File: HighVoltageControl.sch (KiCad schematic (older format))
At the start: 3 parts, among them Q1 DMG2302U, U1 NCS1S1203SC

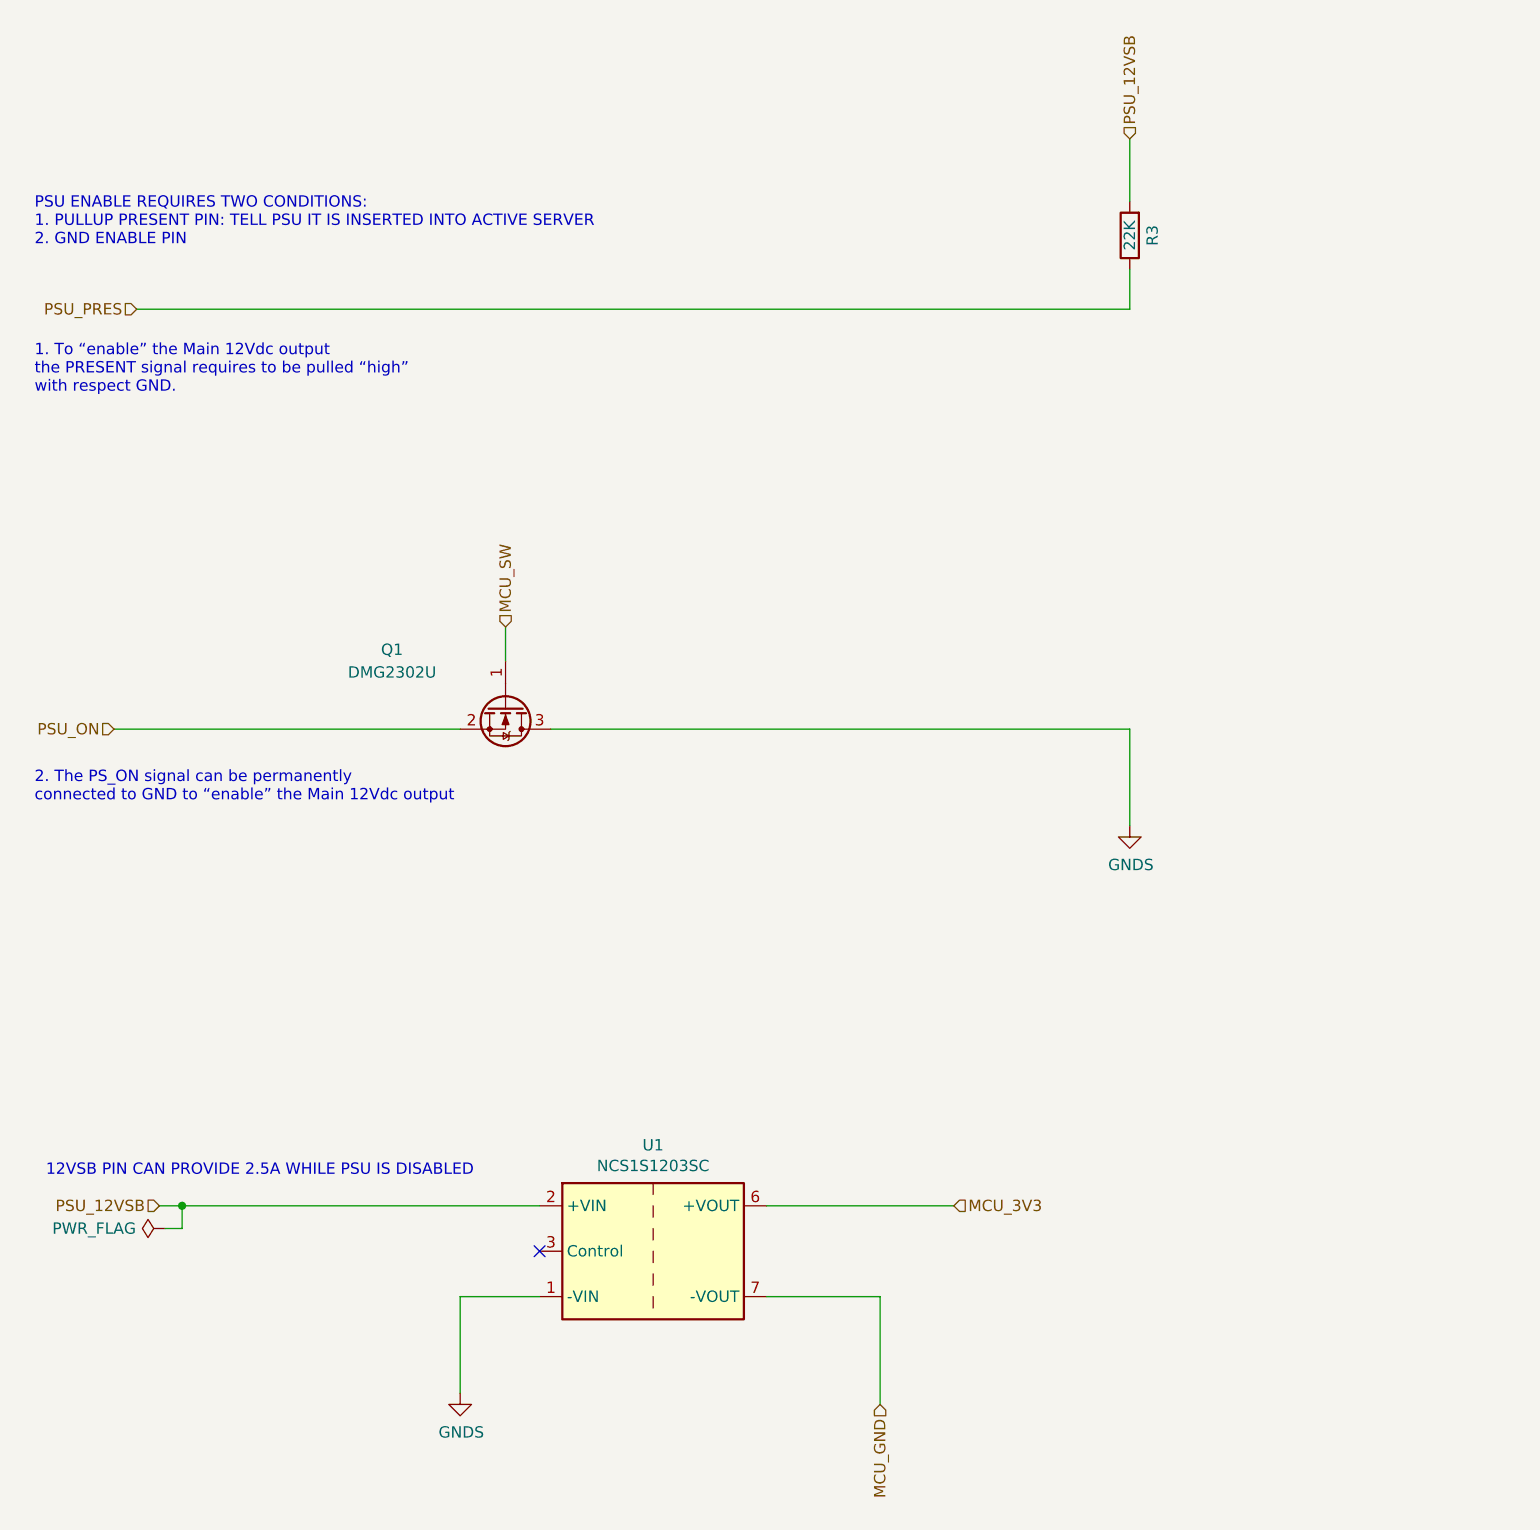
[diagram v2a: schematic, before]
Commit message: Added TFT Delayed Reset sub circuit
changed NCS1S1203SC to NCS1S1205SC
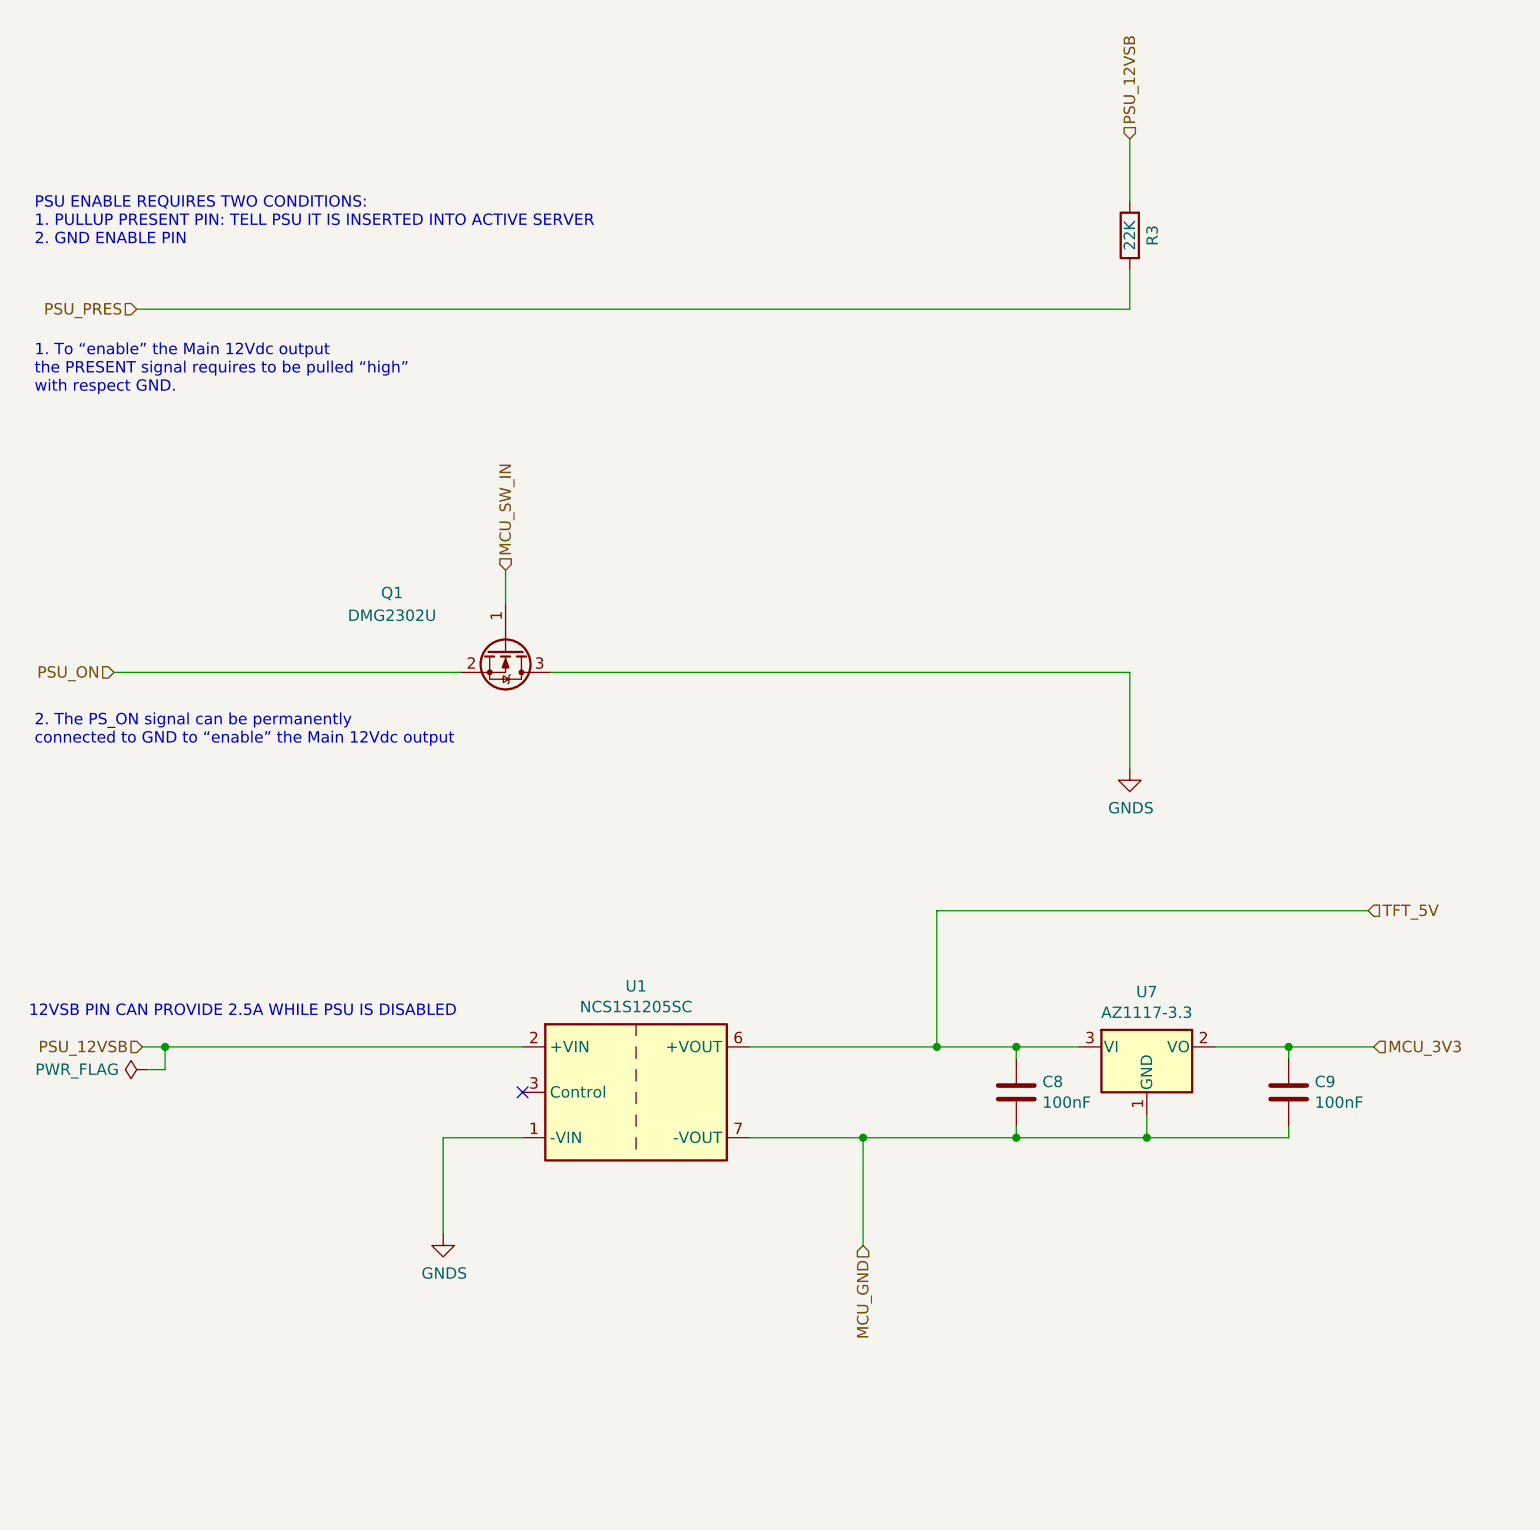
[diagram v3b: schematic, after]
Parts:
- removed U1: NCS1S1203SC, Converter_DCDC:Converter_DCDC_Murata_NCS1SxxxxSC_THT, symbol Converter_DCDC:NCS1S1203SC
- added C8, C9: 100nF, Capacitor_SMD:C_0805_2012Metric_Pad1.15x1.40mm_HandSolder, symbol Device:C
- added U1: NCS1S1205SC, Converter_DCDC:Converter_DCDC_Murata_NCS1SxxxxSC_THT, symbol Converter_DCDC:NCS1S1205SC
- added U7: AZ1117-3.3, Package_TO_SOT_SMD:SOT-89-3_Handsoldering, symbol Regulator_Linear:AZ1117-3.3
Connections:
- net GNDS: now also U1.1 (-VIN)
- net MCU_3V3: now also C9.1, U7.2 (VO)
- net MCU_GND: now also C8.2, C9.2, U1.7 (-VOUT), U7.1 (GND)
- net PSU_12VSB: now also U1.2 (+VIN)
- net MCU_SW renamed MCU_SW_IN
- new net TFT_5V: C8.1, U1.6 (+VOUT), U7.3 (VI)
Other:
- moved on the sheet: Q1
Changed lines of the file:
@@
 $Descr A4 11693 8268
 encoding utf-8
-Sheet 3 5
+Sheet 6 6
 Title ""
 Date ""
@@
 Comment4 ""
 $EndDescr
-Text HLabel 2125 3850 0    50   Input ~ 0
+Text HLabel 2125 3600 0    50   Input ~ 0
 PSU_ON
 Text HLabel 2225 2000 0    50   Input ~ 0
 PSU_PRES
-Text HLabel 5825 5950 2    50   Input ~ 0
+Text HLabel 7675 5250 2    50   Input ~ 0
 MCU_3V3
 Wire Wire Line
-	2125 3850 3650 3850
-Wire Wire Line
-	4050 3850 6600 3850
-$Comp
-L Converter_DCDC:NCS1S1203SC U1
-U 1 1 5F0C9092
-P 4500 6150
-F 0 "U1" H 4500 6617 50  0000 C CNN
-F 1 "NCS1S1203SC" H 4500 6526 50  0000 C CNN
-F 2 "Converter_DCDC:Converter_DCDC_Murata_NCS1SxxxxSC_THT" H 4500 5750 50  0001 C CNN
-F 3 "https://power.murata.com/data/power/ncl/kdc_ncs1.pdf" H 4475 6150 50  0001 C CNN
-	1    4500 6150
-	1    0    0    -1
-$EndComp
-Wire Wire Line
-	4000 5950 2425 5950
-NoConn ~ 4000 6150
-Wire Wire Line
-	4000 6350 3650 6350
-Wire Wire Line
-	3650 6350 3650 6775
+	2125 3600 3650 3600
+Wire Wire Line
+	4050 3600 6600 3600
+Wire Wire Line
+	3925 5250 2350 5250
+NoConn ~ 3925 5450
+Wire Wire Line
+	3925 5650 3575 5650
+Wire Wire Line
+	3575 5650 3575 6075
 $Comp
 L power:GNDS #PWR05
 U 1 1 5F0CC121
-P 3650 6775
-F 0 "#PWR05" H 3650 6525 50  0001 C CNN
-F 1 "GNDS" H 3655 6602 50  0000 C CNN
-F 2 "" H 3650 6775 50  0001 C CNN
-F 3 "" H 3650 6775 50  0001 C CNN
-	1    3650 6775
-	1    0    0    -1
-$EndComp
-Wire Wire Line
-	5000 6350 5500 6350
-Wire Wire Line
-	5500 6350 5500 6825
-Text HLabel 5500 6825 3    50   Input ~ 0
+P 3575 6075
+F 0 "#PWR05" H 3575 5825 50  0001 C CNN
+F 1 "GNDS" H 3580 5902 50  0000 C CNN
+F 2 "" H 3575 6075 50  0001 C CNN
+F 3 "" H 3575 6075 50  0001 C CNN
+	1    3575 6075
+	1    0    0    -1
+$EndComp
+Wire Wire Line
+	4925 5650 5425 5650
+Text HLabel 5425 6125 3    50   Input ~ 0
 MCU_GND
 Wire Wire Line
-	5000 5950 5825 5950
+	4925 5250 5750 5250
 $Comp
 L Device:R R3
@@
 1. To “enable” the Main 12Vdc output \nthe PRESENT signal requires to be pulled “high”\nwith respect GND.
 Wire Wire Line
-	6600 3850 6600 4275
+	6600 3600 6600 4025
 $Comp
 L power:GNDS #PWR0101
 U 1 1 5EFE358D
-P 6600 4275
-F 0 "#PWR0101" H 6600 4025 50  0001 C CNN
-F 1 "GNDS" H 6605 4102 50  0000 C CNN
-F 2 "" H 6600 4275 50  0001 C CNN
-F 3 "" H 6600 4275 50  0001 C CNN
-	1    6600 4275
-	1    0    0    -1
-$EndComp
-Text Notes 1775 4175 0    50   ~ 0
+P 6600 4025
+F 0 "#PWR0101" H 6600 3775 50  0001 C CNN
+F 1 "GNDS" H 6605 3852 50  0000 C CNN
+F 2 "" H 6600 4025 50  0001 C CNN
+F 3 "" H 6600 4025 50  0001 C CNN
+	1    6600 4025
+	1    0    0    -1
+$EndComp
+Text Notes 1775 3925 0    50   ~ 0
 2. The PS_ON signal can be permanently \nconnected to GND to “enable” the Main 12Vdc output
-Text HLabel 2325 5950 0    50   Input ~ 0
+Text HLabel 2250 5250 0    50   Input ~ 0
 PSU_12VSB
 Text Notes 1775 1725 0    50   ~ 0
 PSU ENABLE REQUIRES TWO CONDITIONS:\n1. PULLUP PRESENT PIN: TELL PSU IT IS INSERTED INTO ACTIVE SERVER\n2. GND ENABLE PIN
-Text Notes 1825 5825 0    50   ~ 0
+Text Notes 1750 5125 0    50   ~ 0
 12VSB PIN CAN PROVIDE 2.5A WHILE PSU IS DISABLED
 $Comp
 L power:PWR_FLAG #FLG?
 U 1 1 5EFFE480
-P 2350 6050
+P 2275 5350
 AR Path="/5EFF0F4B/5EFFE480" Ref="#FLG?"  Part="1"
 AR Path="/5F02F4C5/5EFFE480" Ref="#FLG0103"  Part="1"
-F 0 "#FLG0103" H 2350 6125 50  0001 C CNN
-F 1 "PWR_FLAG" V 2350 6178 50  0000 L CNN
-F 2 "" H 2350 6050 50  0001 C CNN
-F 3 "~" H 2350 6050 50  0001 C CNN
-	1    2350 6050
+F 0 "#FLG0103" H 2275 5425 50  0001 C CNN
+F 1 "PWR_FLAG" V 2275 5478 50  0000 L CNN
+F 2 "" H 2275 5350 50  0001 C CNN
+F 3 "~" H 2275 5350 50  0001 C CNN
+	1    2275 5350
 	0    -1   -1   0
 $EndComp
 Wire Wire Line
-	2350 6050 2425 6050
-Wire Wire Line
-	2425 6050 2425 5950
-Connection ~ 2425 5950
-Wire Wire Line
-	2425 5950 2325 5950
+	2275 5350 2350 5350
+Wire Wire Line
+	2350 5350 2350 5250
+Connection ~ 2350 5250
+Wire Wire Line
+	2350 5250 2250 5250
 $Comp
 L Transistor_FET:DMG2302U Q1
 U 1 1 5F001BDB
-P 3850 3750
-F 0 "Q1" V 3600 3250 50  0000 C CNN
-F 1 "DMG2302U" V 3700 3250 50  0000 C CNN
-F 2 "Package_TO_SOT_SMD:SOT-23" H 4050 3675 50  0001 L CIN
-F 3 "http://www.diodes.com/assets/Datasheets/DMG2302U.pdf" H 3850 3750 50  0001 L CNN
-	1    3850 3750
+P 3850 3500
+F 0 "Q1" V 3600 3000 50  0000 C CNN
+F 1 "DMG2302U" V 3700 3000 50  0000 C CNN
+F 2 "Package_TO_SOT_SMD:SOT-23" H 4050 3425 50  0001 L CIN
+F 3 "http://www.diodes.com/assets/Datasheets/DMG2302U.pdf" H 3850 3500 50  0001 L CNN
+	1    3850 3500
 	0    1    1    0
 $EndComp
 Wire Wire Line
-	3850 3550 3850 3400
-Text HLabel 3850 3400 1    50   Input ~ 0
-MCU_SW
+	3850 3300 3850 3150
+Text HLabel 3850 3150 1    50   Input ~ 0
+MCU_SW_IN
+$Comp
+L Converter_DCDC:NCS1S1205SC U1
+U 1 1 5F252162
+P 4425 5450
+F 0 "U1" H 4425 5917 50  0000 C CNN
+F 1 "NCS1S1205SC" H 4425 5826 50  0000 C CNN
+F 2 "Converter_DCDC:Converter_DCDC_Murata_NCS1SxxxxSC_THT" H 4425 5050 50  0001 C CNN
+F 3 "https://power.murata.com/data/power/ncl/kdc_ncs1.pdf" H 4400 5450 50  0001 C CNN
+	1    4425 5450
+	1    0    0    -1
+$EndComp
+$Comp
+L Regulator_Linear:AZ1117-3.3 U7
+U 1 1 5F26009C
+P 6675 5250
+F 0 "U7" H 6675 5492 50  0000 C CNN
+F 1 "AZ1117-3.3" H 6675 5401 50  0000 C CNN
+F 2 "Package_TO_SOT_SMD:SOT-89-3_Handsoldering" H 6675 5500 50  0001 C CIN
+F 3 "https://www.diodes.com/assets/Datasheets/AZ1117.pdf" H 6675 5250 50  0001 C CNN
+	1    6675 5250
+	1    0    0    -1
+$EndComp
+Text HLabel 7650 4650 2    50   Input ~ 0
+TFT_5V
+Wire Wire Line
+	5750 5250 5750 4650
+Wire Wire Line
+	5750 4650 7650 4650
+Wire Wire Line
+	6375 5250 6100 5250
+Connection ~ 5750 5250
+Wire Wire Line
+	6975 5250 7300 5250
+Wire Wire Line
+	6675 5550 6675 5650
+Wire Wire Line
+	6675 5650 6100 5650
+Connection ~ 5425 5650
+Wire Wire Line
+	5425 5650 5425 6125
+$Comp
+L Device:C C8
+U 1 1 5F26AC3D
+P 6100 5450
+F 0 "C8" H 6215 5496 50  0000 L CNN
+F 1 "100nF" H 6215 5405 50  0000 L CNN
+F 2 "Capacitor_SMD:C_0805_2012Metric_Pad1.15x1.40mm_HandSolder" H 6138 5300 50  0001 C CNN
+F 3 "~" H 6100 5450 50  0001 C CNN
+	1    6100 5450
+	1    0    0    -1
+$EndComp
+Wire Wire Line
+	6100 5300 6100 5250
+Connection ~ 6100 5250
+Wire Wire Line
+	6100 5250 5750 5250
+Wire Wire Line
+	6100 5600 6100 5650
+Connection ~ 6100 5650
+Wire Wire Line
+	6100 5650 5425 5650
+$Comp
+L Device:C C9
+U 1 1 5F26CCC7
+P 7300 5450
+F 0 "C9" H 7415 5496 50  0000 L CNN
+F 1 "100nF" H 7415 5405 50  0000 L CNN
+F 2 "Capacitor_SMD:C_0805_2012Metric_Pad1.15x1.40mm_HandSolder" H 7338 5300 50  0001 C CNN
+F 3 "~" H 7300 5450 50  0001 C CNN
+	1    7300 5450
+	1    0    0    -1
+$EndComp
+Wire Wire Line
+	7300 5300 7300 5250
+Wire Wire Line
+	7300 5600 7300 5650
+Wire Wire Line
+	7300 5650 6675 5650
+Connection ~ 6675 5650
+Connection ~ 7300 5250
+Wire Wire Line
+	7300 5250 7675 5250
 $EndSCHEMATC
